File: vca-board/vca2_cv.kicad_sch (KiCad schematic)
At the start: 8 parts, among them U4 TL074

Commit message: VCA components linked
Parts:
- C13: footprint (none) -> Capacitor_SMD:C_0603_1608Metric_Pad1.08x0.95mm_HandSolder; LCSC (none) -> C91367
- D5: footprint (none) -> Diode_SMD:D_SOD-523; LCSC (none) -> C131797
- D6: footprint (none) -> Diode_SMD:D_SOD-123; LCSC (none) -> C81598
- R31: footprint (none) -> Resistor_SMD:R_0201_0603Metric_Pad0.64x0.40mm_HandSolder; LCSC (none) -> C25811
- R34: footprint (none) -> Resistor_SMD:R_0201_0603Metric_Pad0.64x0.40mm_HandSolder; LCSC (none) -> C25803
- R35: LCSC (none) -> C22775
- R36: LCSC (none) -> C25804
- U4: footprint (none) -> Package_SO:SOIC-14_3.9x8.7mm_P1.27mm; LCSC (none) -> C6963
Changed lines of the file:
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@@
+      (effects (font (size 1.27 1.27)) hide)
+    )
+    (property "LCSC" "C25804" (id 4) (at 140.97 60.96 0)
       (effects (font (size 1.27 1.27)) hide)
     )
@@
     (property "Reference" "U4" (id 0) (at 119.38 40.64 0))
     (property "Value" "TL074" (id 1) (at 119.38 43.18 0))
-    (property "Footprint" "" (id 2) (at 118.11 53.34 0)
+    (property "Footprint" "Package_SO:SOIC-14_3.9x8.7mm_P1.27mm" (id 2) (at 118.11 53.34 0)
       (effects (font (size 1.27 1.27)) hide)
     )
     (property "Datasheet" "http://www.ti.com/lit/ds/symlink/tl071.pdf" (id 3) (at 120.65 55.88 0)
+      (effects (font (size 1.27 1.27)) hide)
+    )
+    (property "LCSC" "C6963" (id 4) (at 119.38 50.8 0)
       (effects (font (size 1.27 1.27)) hide)
     )
@@
     (property "Reference" "D6" (id 0) (at 134.62 44.45 0))
     (property "Value" "D" (id 1) (at 134.62 46.99 0))
-    (property "Footprint" "" (id 2) (at 134.62 50.8 0)
+    (property "Footprint" "Diode_SMD:D_SOD-123" (id 2) (at 134.62 50.8 0)
       (effects (font (size 1.27 1.27)) hide)
     )
     (property "Datasheet" "~" (id 3) (at 134.62 50.8 0)
+      (effects (font (size 1.27 1.27)) hide)
+    )
+    (property "LCSC" "C81598" (id 4) (at 134.62 50.8 0)
       (effects (font (size 1.27 1.27)) hide)
     )
@@
       (effects (font (size 1.27 1.27)) (justify left))
     )
-    (property "Footprint" "" (id 2) (at 106.68 66.04 0)
+    (property "Footprint" "Diode_SMD:D_SOD-523" (id 2) (at 106.68 66.04 0)
       (effects (font (size 1.27 1.27)) hide)
     )
     (property "Datasheet" "~" (id 3) (at 106.68 66.04 0)
+      (effects (font (size 1.27 1.27)) hide)
+    )
+    (property "LCSC" "C131797" (id 4) (at 106.68 66.04 0)
       (effects (font (size 1.27 1.27)) hide)
     )
@@
     (property "Reference" "U4" (id 0) (at 83.82 43.18 0))
     (property "Value" "TL074" (id 1) (at 83.82 45.72 0))
-    (property "Footprint" "" (id 2) (at 82.55 55.88 0)
+    (property "Footprint" "Package_SO:SOIC-14_3.9x8.7mm_P1.27mm" (id 2) (at 82.55 55.88 0)
       (effects (font (size 1.27 1.27)) hide)
     )
     (property "Datasheet" "http://www.ti.com/lit/ds/symlink/tl071.pdf" (id 3) (at 85.09 58.42 0)
+      (effects (font (size 1.27 1.27)) hide)
+    )
+    (property "LCSC" "C6963" (id 4) (at 83.82 53.34 0)
       (effects (font (size 1.27 1.27)) hide)
     )
@@
     (property "Reference" "R31" (id 0) (at 68.58 44.45 90))
     (property "Value" "200k" (id 1) (at 68.58 46.99 90))
-    (property "Footprint" "" (id 2) (at 68.58 52.578 90)
+    (property "Footprint" "Resistor_SMD:R_0201_0603Metric_Pad0.64x0.40mm_HandSolder" (id 2) (at 68.58 52.578 90)
       (effects (font (size 1.27 1.27)) hide)
     )
     (property "Datasheet" "~" (id 3) (at 68.58 50.8 0)
+      (effects (font (size 1.27 1.27)) hide)
+    )
+    (property "LCSC" "C25811" (id 4) (at 68.58 50.8 0)
       (effects (font (size 1.27 1.27)) hide)
     )
@@
     (property "Reference" "R34" (id 0) (at 83.82 31.75 90))
     (property "Value" "100k" (id 1) (at 83.82 34.29 90))
-    (property "Footprint" "" (id 2) (at 83.82 39.878 90)
+    (property "Footprint" "Resistor_SMD:R_0201_0603Metric_Pad0.64x0.40mm_HandSolder" (id 2) (at 83.82 39.878 90)
       (effects (font (size 1.27 1.27)) hide)
     )
     (property "Datasheet" "~" (id 3) (at 83.82 38.1 0)
+      (effects (font (size 1.27 1.27)) hide)
+    )
+    (property "LCSC" "C25803" (id 4) (at 83.82 38.1 0)
       (effects (font (size 1.27 1.27)) hide)
     )
@@
     (property "Reference" "C13" (id 0) (at 83.82 17.78 90))
     (property "Value" "10p" (id 1) (at 83.82 20.32 90))
-    (property "Footprint" "" (id 2) (at 87.63 24.4348 0)
+    (property "Footprint" "Capacitor_SMD:C_0603_1608Metric_Pad1.08x0.95mm_HandSolder" (id 2) (at 87.63 24.4348 0)
       (effects (font (size 1.27 1.27)) hide)
     )
     (property "Datasheet" "~" (id 3) (at 83.82 25.4 0)
+      (effects (font (size 1.27 1.27)) hide)
+    )
+    (property "LCSC" "C91367" (id 4) (at 83.82 25.4 0)
       (effects (font (size 1.27 1.27)) hide)
     )
@@
       (effects (font (size 1.27 1.27)) hide)
     )
+    (property "LCSC" "C22775" (id 4) (at 99.06 53.34 0)
+      (effects (font (size 1.27 1.27)) hide)
+    )

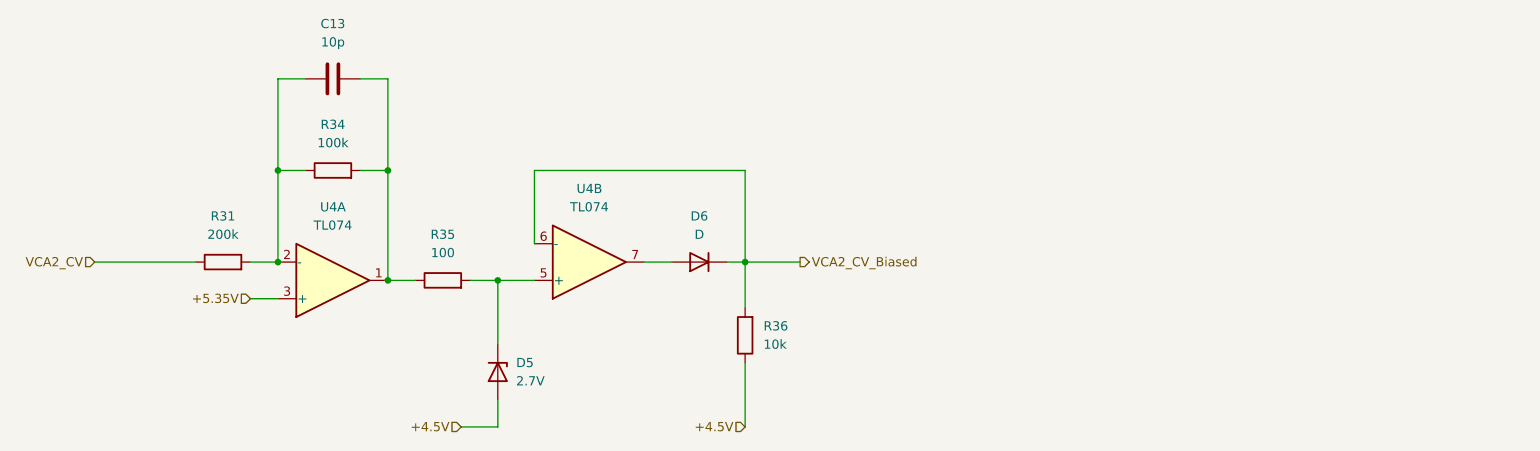
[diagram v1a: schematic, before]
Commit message: VCA board components placed
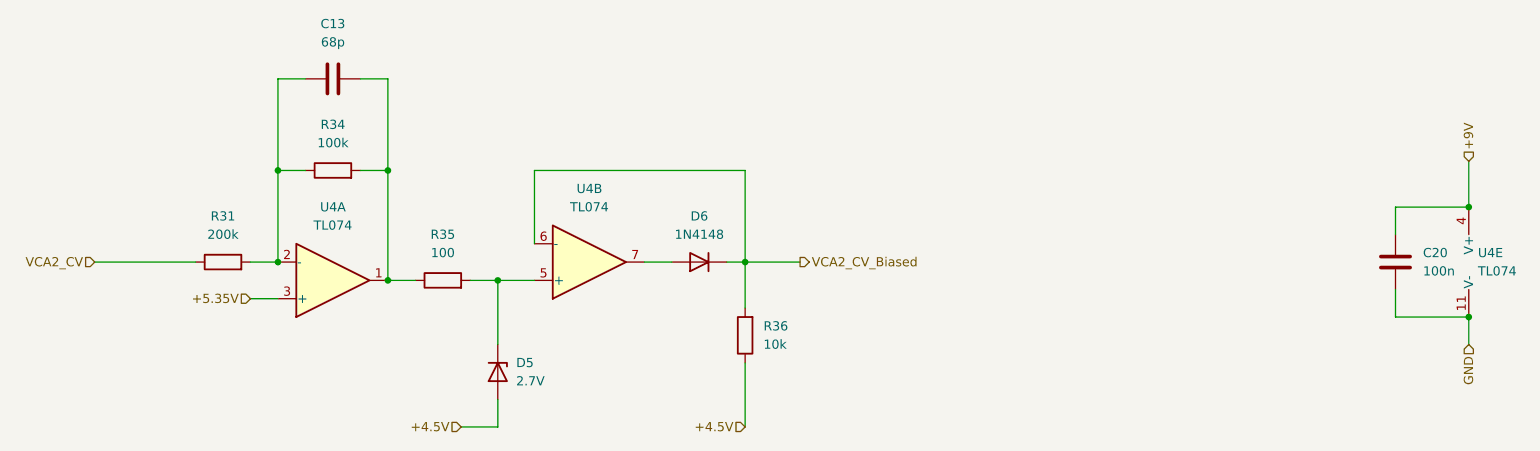
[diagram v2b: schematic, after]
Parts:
- added C20: 100n, Capacitor_SMD:C_0603_1608Metric_Pad1.08x0.95mm_HandSolder, symbol Device:C
- added unit 5 of U4
- C13: value 10p -> 68p; LCSC C91367 -> C1680
- D5: footprint Diode_SMD:D_SOD-523 -> Diode_SMD:D_SOD-123; LCSC C131797 -> C406712
- D6: value D -> 1N4148
- R31, R34: footprint Resistor_SMD:R_0201_0603Metric_Pad0.64x0.40mm_HandSolder -> Resistor_SMD:R_0603_1608Metric_Pad0.98x0.95mm_HandSolder
- R35, R36: footprint (none) -> Resistor_SMD:R_0603_1608Metric_Pad0.98x0.95mm_HandSolder
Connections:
- new net +9V: C20.2, U4.4 (V+)
- new net GND: C20.1, U4.11 (V-)
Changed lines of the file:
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@@
 (kicad_sch (version 20211123) (generator eeschema)
   (paper "A4")
+  (junction (at 241.3 43.18) (diameter 0) (color 0 0 0 0)
+  )
   (junction (at 140.97 50.8) (diameter 0) (color 0 0 0 0)
   )
@@
   (junction (at 76.2 50.8) (diameter 0) (color 0 0 0 0)
   )
+  (junction (at 241.3 58.42) (diameter 0) (color 0 0 0 0)
+  )
   (wire (pts (xy 72.39 50.8) (xy 76.2 50.8))
     (stroke (width 0) (type default) (color 0 0 0 0))
   )
+  (wire (pts (xy 231.14 54.61) (xy 231.14 58.42))
+    (stroke (width 0) (type default) (color 0 0 0 0))
+  )
   (wire (pts (xy 140.97 50.8) (xy 140.97 38.1))
     (stroke (width 0) (type default) (color 0 0 0 0))
   )
+  (wire (pts (xy 231.14 58.42) (xy 241.3 58.42))
+    (stroke (width 0) (type default) (color 0 0 0 0))
+  )
   (wire (pts (xy 140.97 64.77) (xy 140.97 73.66))
     (stroke (width 0) (type default) (color 0 0 0 0))
@@
     (stroke (width 0) (type default) (color 0 0 0 0))
   )
+  (wire (pts (xy 241.3 36.83) (xy 241.3 43.18))
+    (stroke (width 0) (type default) (color 0 0 0 0))
+  )
   (wire (pts (xy 106.68 53.34) (xy 106.68 62.23))
     (stroke (width 0) (type default) (color 0 0 0 0))
@@
     (stroke (width 0) (type default) (color 0 0 0 0))
   )
+  (wire (pts (xy 241.3 58.42) (xy 241.3 62.23))
+    (stroke (width 0) (type default) (color 0 0 0 0))
+  )
   (wire (pts (xy 91.44 53.34) (xy 95.25 53.34))
     (stroke (width 0) (type default) (color 0 0 0 0))
   )
+  (wire (pts (xy 241.3 43.18) (xy 231.14 43.18))
+    (stroke (width 0) (type default) (color 0 0 0 0))
+  )
   (wire (pts (xy 91.44 38.1) (xy 91.44 53.34))
     (stroke (width 0) (type default) (color 0 0 0 0))
@@
     (stroke (width 0) (type default) (color 0 0 0 0))
   )
+  (wire (pts (xy 231.14 43.18) (xy 231.14 46.99))
+    (stroke (width 0) (type default) (color 0 0 0 0))
+  )
   (wire (pts (xy 76.2 25.4) (xy 76.2 38.1))
     (stroke (width 0) (type default) (color 0 0 0 0))
@@
   (hierarchical_label "+5.35V" (shape input) (at 72.39 55.88 180)
     (effects (font (size 1.27 1.27)) (justify right))
+  )
+  (hierarchical_label "+9V" (shape input) (at 241.3 36.83 90)
+    (effects (font (size 1.27 1.27)) (justify left))
   )
   (hierarchical_label "+4.5V" (shape input) (at 101.6 73.66 180)
@@
     (effects (font (size 1.27 1.27)) (justify left))
   )
+  (hierarchical_label "GND" (shape input) (at 241.3 62.23 270)
+    (effects (font (size 1.27 1.27)) (justify right))
+  )
+  (symbol (lib_id "Device:C") (at 231.14 50.8 180) (unit 1)
+    (in_bom yes) (on_board yes) (fields_autoplaced)
+    (property "Reference" "C20" (id 0) (at 234.95 49.5299 0)
+      (effects (font (size 1.27 1.27)) (justify right))
+    )
+    (property "Value" "100n" (id 1) (at 234.95 52.0699 0)
+      (effects (font (size 1.27 1.27)) (justify right))
+    )
+    (property "Footprint" "Capacitor_SMD:C_0603_1608Metric_Pad1.08x0.95mm_HandSolder" (id 2) (at 230.1748 46.99 0)
+      (effects (font (size 1.27 1.27)) hide)
+    )
+    (property "Datasheet" "~" (id 3) (at 231.14 50.8 0)
+      (effects (font (size 1.27 1.27)) hide)
+    )
+    (property "LCSC" "C76711" (id 4) (at 231.14 50.8 0)
+      (effects (font (size 1.27 1.27)) hide)
+    )
+    (pin "1")
+    (pin "2")
+  )
   (symbol (lib_id "Device:R") (at 140.97 60.96 180) (unit 1)
     (in_bom yes) (on_board yes) (fields_autoplaced)
@@
       (effects (font (size 1.27 1.27)) (justify right))
     )
-    (property "Footprint" "" (id 2) (at 142.748 60.96 90)
+    (property "Footprint" "Resistor_SMD:R_0603_1608Metric_Pad0.98x0.95mm_HandSolder" (id 2) (at 142.748 60.96 90)
       (effects (font (size 1.27 1.27)) hide)
     )
@@
     (in_bom yes) (on_board yes) (fields_autoplaced)
     (property "Reference" "D6" (id 0) (at 134.62 44.45 0))
-    (property "Value" "D" (id 1) (at 134.62 46.99 0))
+    (property "Value" "1N4148" (id 1) (at 134.62 46.99 0))
     (property "Footprint" "Diode_SMD:D_SOD-123" (id 2) (at 134.62 50.8 0)
       (effects (font (size 1.27 1.27)) hide)
@@
       (effects (font (size 1.27 1.27)) (justify left))
     )
-    (property "Footprint" "Diode_SMD:D_SOD-523" (id 2) (at 106.68 66.04 0)
+    (property "Footprint" "Diode_SMD:D_SOD-123" (id 2) (at 106.68 66.04 0)
       (effects (font (size 1.27 1.27)) hide)
     )
@@
       (effects (font (size 1.27 1.27)) hide)
     )
-    (property "LCSC" "C131797" (id 4) (at 106.68 66.04 0)
+    (property "LCSC" "C406712" (id 4) (at 106.68 66.04 0)
       (effects (font (size 1.27 1.27)) hide)
     )
@@
     (property "Reference" "R31" (id 0) (at 68.58 44.45 90))
     (property "Value" "200k" (id 1) (at 68.58 46.99 90))
-    (property "Footprint" "Resistor_SMD:R_0201_0603Metric_Pad0.64x0.40mm_HandSolder" (id 2) (at 68.58 52.578 90)
+    (property "Footprint" "Resistor_SMD:R_0603_1608Metric_Pad0.98x0.95mm_HandSolder" (id 2) (at 68.58 52.578 90)
       (effects (font (size 1.27 1.27)) hide)
     )
@@
     (pin "1")
     (pin "2")
+  )
+  (symbol (lib_id "Amplifier_Operational:TL074") (at 243.84 50.8 0) (unit 5)
+    (in_bom yes) (on_board yes) (fields_autoplaced)
+    (property "Reference" "U4" (id 0) (at 242.57 49.5299 0)
+      (effects (font (size 1.27 1.27)) (justify left))
+    )
+    (property "Value" "TL074" (id 1) (at 242.57 52.0699 0)
+      (effects (font (size 1.27 1.27)) (justify left))
+    )
+    (property "Footprint" "Package_SO:SOIC-14_3.9x8.7mm_P1.27mm" (id 2) (at 242.57 48.26 0)
+      (effects (font (size 1.27 1.27)) hide)
+    )
+    (property "Datasheet" "http://www.ti.com/lit/ds/symlink/tl071.pdf" (id 3) (at 245.11 45.72 0)
+      (effects (font (size 1.27 1.27)) hide)
+    )
+    (property "LCSC" "C6963" (id 4) (at 243.84 50.8 0)
+      (effects (font (size 1.27 1.27)) hide)
+    )
+    (pin "1")
+    (pin "2")
+    (pin "3")
+    (pin "5")
+    (pin "6")
+    (pin "7")
+    (pin "10")
+    (pin "8")
+    (pin "9")
+    (pin "12")
+    (pin "13")
+    (pin "14")
+    (pin "11")
+    (pin "4")
   )
   (symbol (lib_id "Device:R") (at 83.82 38.1 90) (unit 1)
@@
     (property "Reference" "R34" (id 0) (at 83.82 31.75 90))
     (property "Value" "100k" (id 1) (at 83.82 34.29 90))
-    (property "Footprint" "Resistor_SMD:R_0201_0603Metric_Pad0.64x0.40mm_HandSolder" (id 2) (at 83.82 39.878 90)
+    (property "Footprint" "Resistor_SMD:R_0603_1608Metric_Pad0.98x0.95mm_HandSolder" (id 2) (at 83.82 39.878 90)
       (effects (font (size 1.27 1.27)) hide)
     )
@@
     (in_bom yes) (on_board yes) (fields_autoplaced)
     (property "Reference" "C13" (id 0) (at 83.82 17.78 90))
-    (property "Value" "10p" (id 1) (at 83.82 20.32 90))
+    (property "Value" "68p" (id 1) (at 83.82 20.32 90))
     (property "Footprint" "Capacitor_SMD:C_0603_1608Metric_Pad1.08x0.95mm_HandSolder" (id 2) (at 87.63 24.4348 0)
       (effects (font (size 1.27 1.27)) hide)
@@
       (effects (font (size 1.27 1.27)) hide)
     )
-    (property "LCSC" "C91367" (id 4) (at 83.82 25.4 0)
+    (property "LCSC" "C1680" (id 4) (at 83.82 25.4 0)
       (effects (font (size 1.27 1.27)) hide)
     )
@@
     (property "Reference" "R35" (id 0) (at 99.06 46.99 90))
     (property "Value" "100" (id 1) (at 99.06 49.53 90))
-    (property "Footprint" "" (id 2) (at 99.06 55.118 90)
-      (effects (font (size 1.27 1.27)) hide)
-    )
+    (property "Footprint" "Resistor_SMD:R_0603_1608Metric_Pad0.98x0.95mm_HandSolder" (id 2) (at 99.06 55.118 90)
+      (effects (font (size 1.27 1.27)) hide)
+    )

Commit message: Remove D from linear VCA + update graphics
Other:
- company: (none) -> Pedal Markt / Andrey Salomatin
- title: (none) -> VCA Board
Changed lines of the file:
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@@
 (kicad_sch (version 20211123) (generator eeschema)
   (paper "A4")
+  (title_block
+    (title "VCA Board")
+    (date "2024-11-07")
+    (rev "v1rev2")
+    (company "Pedal Markt / Andrey Salomatin")
+  )
   (junction (at 241.3 43.18) (diameter 0) (color 0 0 0 0)
   )

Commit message: wip pre-redo orientation
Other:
- company: Pedal Markt / Andrey Salomatin -> Andrey Salomatin / Pedal Markt
- title: VCA Board -> Mag
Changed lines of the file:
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@@
   (paper "A4")
   (title_block
-    (title "VCA Board")
+    (title "Mag")
     (date "2024-11-07")
     (rev "v1rev2")
-    (company "Pedal Markt / Andrey Salomatin")
+    (company "Andrey Salomatin / Pedal Markt")
   )
   (junction (at 241.3 43.18) (diameter 0) (color 0 0 0 0)
